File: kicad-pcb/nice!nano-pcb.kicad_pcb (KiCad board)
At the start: 2 copper layers, 14 parts, among them J1 Conn_Coaxial, SW1 SW_Push, SW2 SW_Push, SW3 SW_Nidec_CAS-120A1, U1 nice_nano, U2 LoRa-E220-900M22S

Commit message: Setup fill ground, small fixes
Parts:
- moved C4 0.32 mm to (181.3, 99.2)
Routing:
- net BAT_GND: track 45.3 -> 53.8 mm
- net UBTN: track 0.00 -> 6.17 mm
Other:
- board outline added: 88 x 42.2 mm
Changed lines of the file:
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@@
 		)
 		(embedded_fonts no)
-		(model "${KIPRJMOD}/additional-symbols/LoRa_Radio.pretty/LoRa-E220-900M.x3d"
+		(model "./LoRa-E220-900M.x3d"
 			(offset
 				(xyz 0 0 0)
@@
 	(footprint "Capacitor_SMD:C_1206_3216Metric_Pad1.33x1.80mm_HandSolder"
 		(layer "F.Cu")
-		(at 180.97 99.2 -90)
+		(at 181.29 99.2 -90)
 		(descr "Capacitor SMD 1206 (3216 Metric), square (rectangular) end terminal, IPC-7351 nominal with elongated pad for handsoldering. (Body size source: IPC-SM-782 page 76, https://www.pcb-3d.com/wordpress/wp-content/uploads/ipc-sm-782a_amendment_1_and_2.pdf), generated with kicad-footprint-generator")
 		(tags "capacitor handsolder")
@@
 	)
 	(footprint "Battery:BatteryHolder_Keystone_1042_1x18650"
+		(locked yes)
 		(layer "B.Cu")
 		(at 162.69 110.5 180)
@@
 	)
 	(footprint "Battery:BatteryHolder_Keystone_1042_1x18650"
+		(locked yes)
 		(layer "B.Cu")
 		(at 162.69 90.15 180)
@@
 		)
 		(fill no)
-		(layer "F.CrtYd")
+		(locked yes)
+		(layer "Edge.Cuts")
 	)
 	(gr_text "115"
@@
 		)
 	)
+	(dimension
+		(type orthogonal)
+		(layer "User.1")
+		(pts
+			(xy 118.53 79.32) (xy 118.5 121.5)
+		)
+		(height -4.11)
+		(orientation 1)
+		(format
+			(prefix "")
+			(suffix "")
+			(units 3)
+			(units_format 0)
+			(precision 4)
+			(suppress_zeroes yes)
+		)
+		(style
+			(thickness 0.1)
+			(arrow_length 1.27)
+			(text_position_mode 0)
+			(arrow_direction outward)
+			(extension_height 0.58642)
+			(extension_offset 0.5)
+			(keep_text_aligned yes)
+		)
+		(gr_text "42.18"
+			(at 113.27 100.41 90)
+			(layer "User.1")
+			(effects
+				(font
+					(size 1 1)
+					(thickness 0.15)
+				)
+			)
+		)
+	)
 	(segment
 		(start 178.51 92.81)
@@
 	)
 	(segment
-		(start 182.8 91.7)
-		(end 182.8 93.975)
+		(start 181.29 97.3175)
+		(end 181.29 97.6375)
 		(width 0.8)
 		(layer "F.Cu")
@@
 	)
 	(segment
-		(start 180.94 95.835)
-		(end 180.94 97.6075)
+		(start 173 90.0625)
+		(end 173.5325 89.53)
 		(width 0.8)
 		(layer "F.Cu")
@@
 	)
 	(segment
-		(start 169.74 91.04)
-		(end 172.0225 91.04)
-		(width 1.1)
+		(start 173.5325 89.53)
+		(end 181.08 89.53)
+		(width 0.8)
 		(layer "F.Cu")
 		(net 4)
 	)
 	(segment
-		(start 180.97 97.6375)
-		(end 186.7175 97.6375)
+		(start 181.08 89.53)
+		(end 182.8 91.25)
 		(width 0.8)
 		(layer "F.Cu")
@@
 	)
 	(segment
-		(start 173.2525 89.81)
-		(end 180.91 89.81)
-		(width 0.8)
+		(start 169.74 91.04)
+		(end 172.0225 91.04)
+		(width 1.1)
 		(layer "F.Cu")
 		(net 4)
@@
 	(segment
 		(start 182.575 94.2)
-		(end 180.94 95.835)
+		(end 181.31 95.465)
 		(width 0.8)
 		(layer "F.Cu")
@@
 	)
 	(segment
-		(start 186.7175 97.6375)
-		(end 191.89 102.81)
+		(start 181.31 95.465)
+		(end 181.31 97.2975)
+		(width 0.8)
+		(layer "F.Cu")
+		(net 4)
+	)
+	(segment
+		(start 182.8 91.25)
+		(end 182.8 93.975)
 		(width 0.8)
 		(layer "F.Cu")
@@
 	)
 	(segment
-		(start 191.89 102.81)
-		(end 197.82 102.81)
+		(start 181.29 97.6375)
+		(end 186.7175 97.6375)
 		(width 0.8)
 		(layer "F.Cu")
@@
 	)
 	(segment
-		(start 180.94 97.6075)
-		(end 180.97 97.6375)
+		(start 191.89 102.81)
+		(end 197.82 102.81)
 		(width 0.8)
 		(layer "F.Cu")
@@
 	)
 	(segment
-		(start 182.8 93.975)
-		(end 182.575 94.2)
+		(start 186.7175 97.6375)
+		(end 191.89 102.81)
 		(width 0.8)
 		(layer "F.Cu")
@@
 	)
 	(segment
-		(start 180.91 89.81)
-		(end 182.8 91.7)
+		(start 181.31 97.2975)
+		(end 181.29 97.3175)
 		(width 0.8)
 		(layer "F.Cu")
@@
 	)
 	(segment
-		(start 173 90.0625)
-		(end 173.2525 89.81)
+		(start 182.8 93.975)
+		(end 182.575 94.2)
 		(width 0.8)
 		(layer "F.Cu")
@@
 		(start 182.9175 80.88)
 		(end 169.74 80.88)
-		(width 1.1)
+		(width 1.6)
 		(layer "F.Cu")
 		(net 5)
@@
 		(start 187.9625 85.925)
 		(end 182.9175 80.88)
-		(width 1.1)
+		(width 1.6)
 		(layer "F.Cu")
 		(net 5)
@@
 		(start 187.9625 87.5)
 		(end 187.9625 85.925)
-		(width 1.1)
+		(width 1.6)
 		(layer "F.Cu")
 		(net 5)
@@
 		(start 189.9625 85.5)
 		(end 187.9625 87.5)
-		(width 1.1)
+		(width 1.6)
 		(layer "F.Cu")
 		(net 5)
@@
 		(start 191.5 81.5)
 		(end 191.5 84)
-		(width 1.1)
+		(width 1.6)
 		(layer "F.Cu")
 		(net 5)
@@
 		(start 190 85.5)
 		(end 189.9625 85.5)
-		(width 1.1)
+		(width 1.6)
 		(layer "F.Cu")
 		(net 5)
@@
 		(start 191.5 84)
 		(end 190 85.5)
-		(width 1.1)
+		(width 1.6)
 		(layer "F.Cu")
 		(net 5)
@@
 	)
 	(segment
+		(start 149.56 100.78)
+		(end 152.52 103.74)
+		(width 0.8)
+		(layer "F.Cu")
+		(net 13)
+	)
+	(segment
+		(start 152.52 103.74)
+		(end 154.5 103.74)
+		(width 0.8)
+		(layer "F.Cu")
+		(net 13)
+	)
+	(segment
 		(start 193.75 106.62)
 		(end 197.82 106.62)
@@
 	)
 	(segment
-		(start 181.4625 100.27)
-		(end 183.82 100.27)
-		(width 0.9)
-		(layer "F.Cu")
-		(net 19)
-	)
-	(segment
 		(start 177 85.31)
 		(end 177 85.19)
@@
 	)
 	(segment
-		(start 183.82 114.73)
-		(end 185.87 114.73)
-		(width 0.9)
-		(layer "F.Cu")
-		(net 19)
-	)
-	(segment
 		(start 169.74 85.96)
 		(end 172.0225 85.96)
@@
 	)
 	(segment
-		(start 185.46 100.27)
-		(end 185.67 100.48)
-		(width 0.9)
+		(start 180.97 100.7625)
+		(end 181.3685 100.364)
+		(width 0.8)
 		(layer "F.Cu")
 		(net 19)
@@
 	)
 	(segment
-		(start 183.82 114.73)
-		(end 182.14 114.73)
-		(width 0.9)
-		(layer "F.Cu")
-		(net 19)
-	)
-	(segment
 		(start 197.82 94.63)
 		(end 197.84 94.61)
@@
 	)
 	(segment
-		(start 183.82 100.27)
-		(end 185.46 100.27)
-		(width 0.9)
-		(layer "F.Cu")
-		(net 19)
-	)
-	(segment
 		(start 172.0225 85.96)
 		(end 173 86.9375)
@@
 	)
 	(segment
-		(start 180.97 100.7625)
-		(end 181.4625 100.27)
+		(start 183.82 114.73)
+		(end 187.37 114.73)
 		(width 0.9)
 		(layer "F.Cu")
@@
 	)
 	(segment
+		(start 185.584 100.364)
+		(end 190.25 105.03)
+		(width 0.8)
+		(layer "F.Cu")
+		(net 19)
+	)
+	(segment
+		(start 182 114.73)
+		(end 181.65 115.08)
+		(width 0.9)
+		(layer "F.Cu")
+		(net 19)
+	)
+	(segment
 		(start 197.84 94.61)
 		(end 197.84 93.55)
@@
 	)
 	(segment
+		(start 181.3685 100.364)
+		(end 185.584 100.364)
+		(width 0.8)
+		(layer "F.Cu")
+		(net 19)
+	)
+	(segment
 		(start 175.5 86.69)
 		(end 173.2475 86.69)
@@
 		(net 19)
 	)
+	(segment
+		(start 183.82 114.73)
+		(end 182 114.73)
+		(width 0.9)
+		(layer "F.Cu")
+		(net 19)
+	)
 	(via
 		(at 120.8 90.15)
@@
 		(layer "F.Cu")
 		(hatch edge 0.5)
-		(connect_pads
-			(clearance 0.5)
+		(connect_pads yes
+			(clearance 0.65)
 		)
-		(min_thickness 0.25)
+		(min_thickness 0.65)
 		(filled_areas_thickness no)
 		(fill yes
@@
 	)
 	(group ""
+		(locked yes)
 		(members "0d25d8d0-e026-41a7-8a83-71a4843b173f" "2d0b756e-706a-4929-9fa2-3bc940ccf22a")
 	)

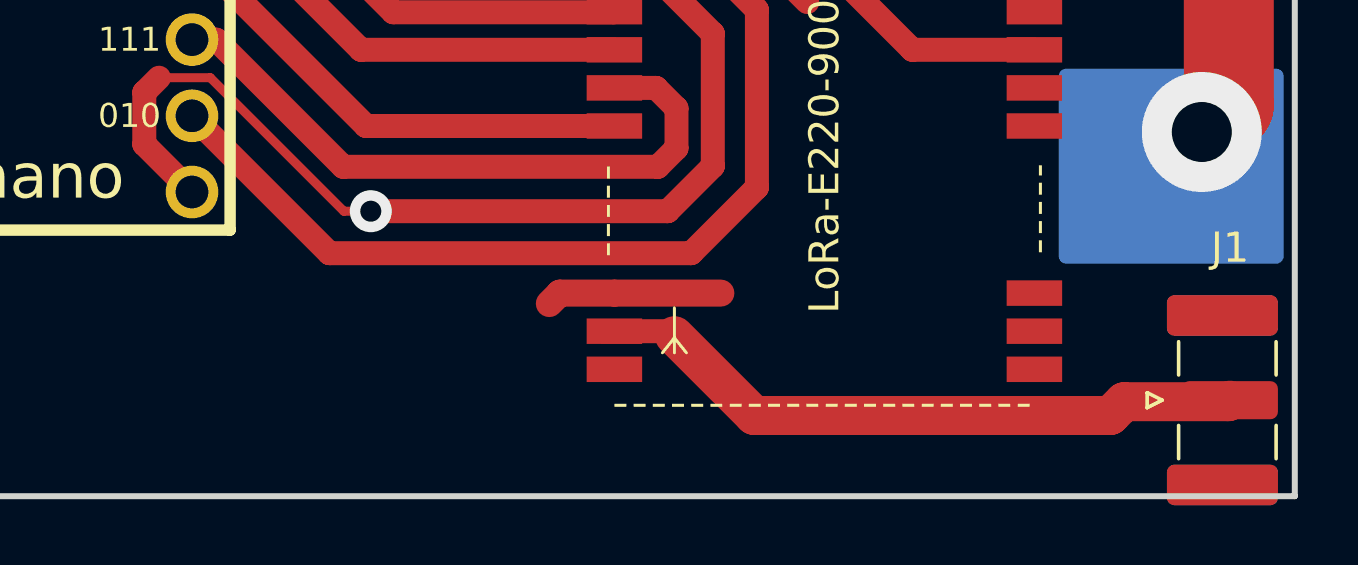
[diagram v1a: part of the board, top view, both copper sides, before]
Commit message: Move antenna coaxial
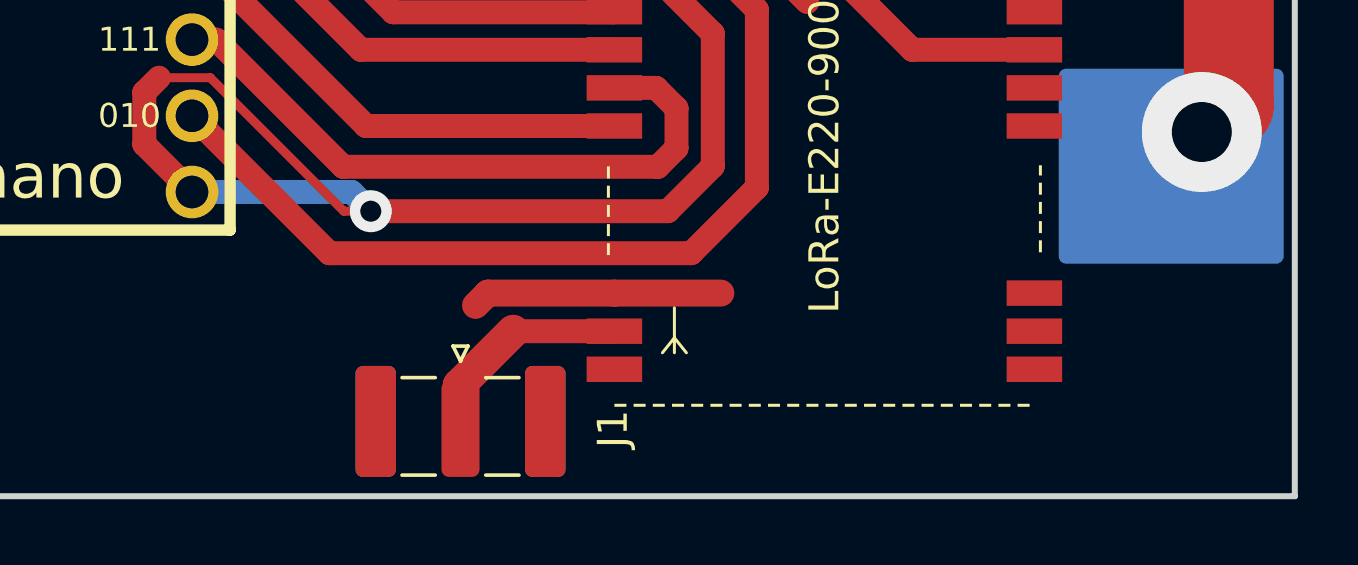
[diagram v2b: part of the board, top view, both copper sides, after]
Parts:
- moved J1 25.7 mm to (178.7, 119.3), turned to -90 degrees
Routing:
- net ANT: track 22.3 -> 7.39 mm
- net NRST: track 34.1 -> 40.4 mm
- net BAT_GND: track 53.8 -> 56.3 mm

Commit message: Final edits
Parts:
- added U3: TFT_320x240, ST7789:TFT-240x320-2.4, F.Cu at (128.0, 100.4)
- added U4: LX-LC535, LX-LC535:LX-LC535, F.Cu at (142.1, 89.8)
- moved SW1 33.2 mm to (122.4, 116.8)
- moved R_ADC_B1 1.64 mm to (176.2, 94.3)
- moved R_ADC_T1 0.93 mm to (179.3, 84.0)
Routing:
- net BAT_GND: track 56.3 -> 201.9 mm, vias 1 -> 3
- net MISO: track 16.9 -> 96.1 mm, vias 0 -> 2
- net BAT_RAW_VCC: track 30.3 -> 103.9 mm, vias 2 -> 3
- net P1.06: track 0.00 -> 69.8 mm
- net MOSI: track 16.3 -> 77.8 mm
- net SCK: track 21.8 -> 80.8 mm
- net P1.07: track 0.00 -> 52.5 mm
- net P1.02: track 0.00 -> 50.5 mm
- net P1.01: track 0.00 -> 48.5 mm
- net UBTN: track 6.17 -> 50.3 mm, vias 0 -> 1
- net VCC: track 40.1 -> 83.5 mm, vias 0 -> 1
- net BATT: track 10.5 -> 9.87 mm
